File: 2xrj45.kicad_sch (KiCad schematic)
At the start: 20 parts, among them J1 Bus_RJ45_JTH-0024NL, J2 Bus_RJ45_JTH-0024NL

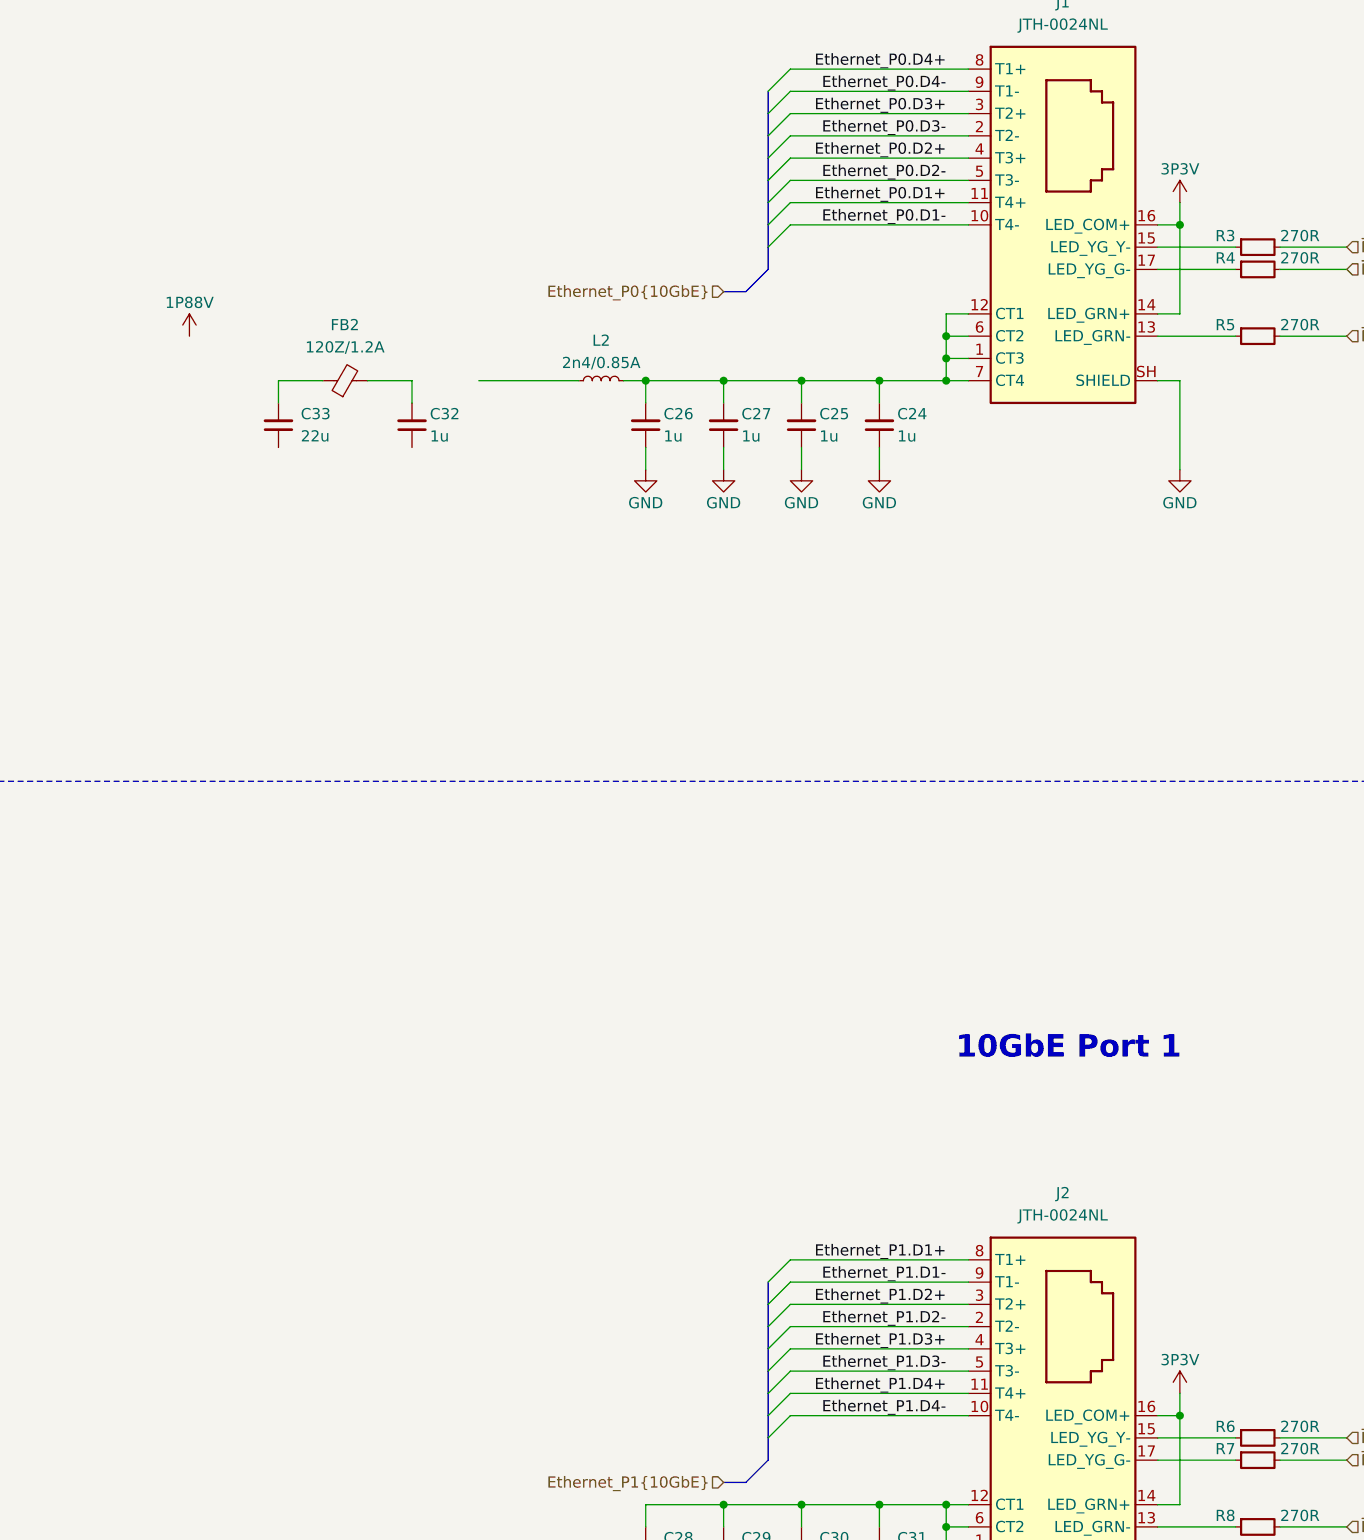
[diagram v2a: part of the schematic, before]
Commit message: [#80813] Change 3V3 and 1V88 power rails names
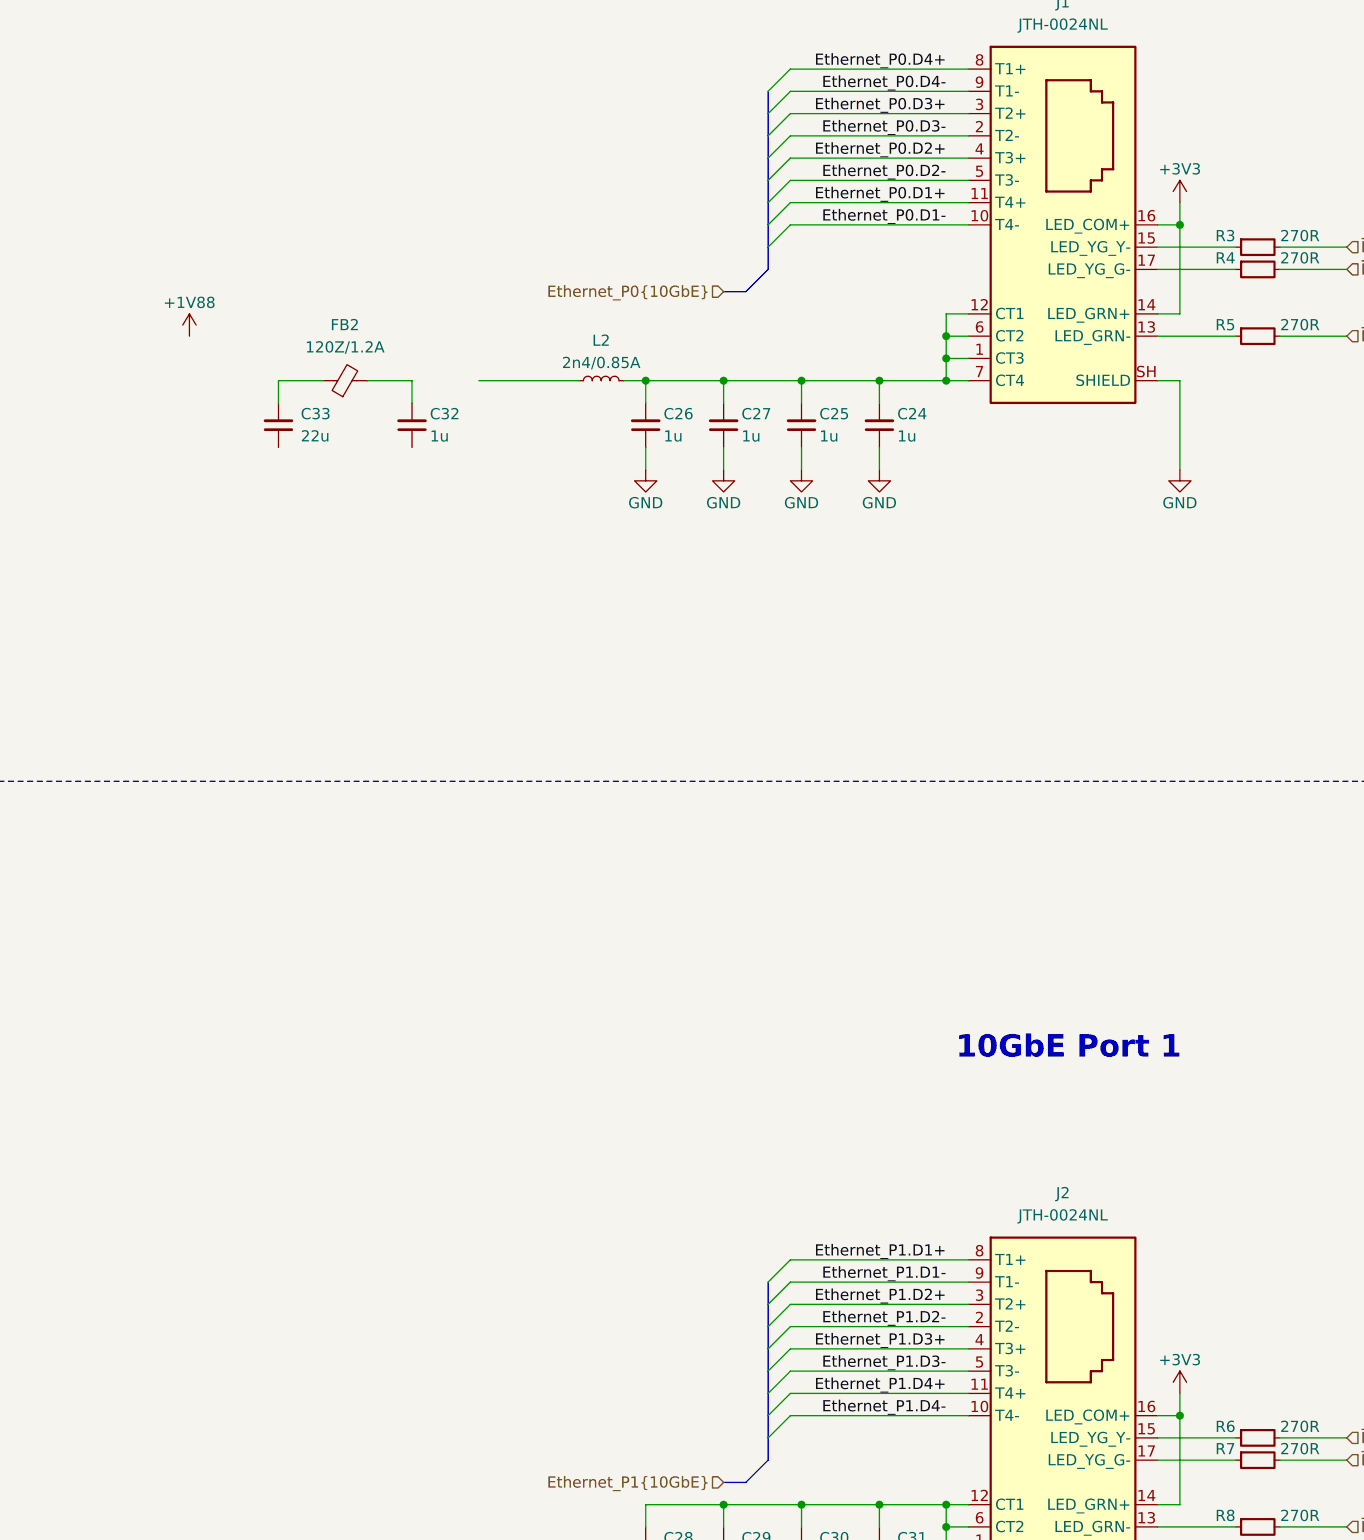
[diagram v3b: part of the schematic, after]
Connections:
- net 3P3V renamed +3V3
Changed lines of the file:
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@@
-	)
-	(symbol
-		(lib_id "antmicropower:VDD")
-		(at 115.57 92.71 0)
-		(unit 1)
-		(exclude_from_sim no)
-		(in_bom yes)
-		(on_board yes)
-		(dnp no)
-		(property "Reference" "#PWR0127"
-			(at 115.57 96.52 0)
-			(effects
-				(font
-					(size 1.27 1.27)
-				)
-				(hide yes)
-			)
-		)
-		(property "Value" "1P88V"
-			(at 115.57 88.9 0)
-			(effects
-				(font
-					(size 1.27 1.27)
-				)
-			)
-		)
-		(property "Footprint" ""
-			(at 115.57 92.71 0)
-			(effects
-				(font
-					(size 1.27 1.27)
-				)
-				(hide yes)
-			)
-		)
-		(property "Datasheet" ""
-			(at 115.57 92.71 0)
-			(effects
-				(font
-					(size 1.27 1.27)
-				)
-				(hide yes)
-			)
-		)
-		(property "Description" ""
-			(at 115.57 92.71 0)
-			(effects
-				(font
-					(size 1.27 1.27)
-				)
-				(hide yes)
-			)
-		)
-		(pin "1"
-		)
-		(instances
-			(project "10-gbe-expansion"
-				(path "/04bda987-e5eb-48b4-9e90-d8211dc11b39/b3dd2e9f-aefc-4b19-a6a4-069fdee319cd"
-					(reference "#PWR0127")
-					(unit 1)
-				)
-			)
-		)
 	)
 	(symbol
@@
 	)
 	(symbol
-		(lib_id "antmicropower:VCC")
-		(at 228.6 77.47 0)
+		(lib_id "antmicropower:+1V8")
+		(at 115.57 92.71 0)
 		(unit 1)
 		(exclude_from_sim no)
@@
 		(on_board yes)
 		(dnp no)
-		(property "Reference" "#PWR04"
-			(at 228.6 81.28 0)
-			(effects
-				(font
-					(size 1.27 1.27)
-				)
-				(hide yes)
-			)
-		)
-		(property "Value" "3P3V"
-			(at 228.6 73.66 0)
-			(effects
-				(font
-					(size 1.27 1.27)
+		(property "Reference" "#PWR014"
+			(at 130.81 95.25 0)
+			(effects
+				(font
+					(size 1.27 1.27)
+					(thickness 0.15)
+				)
+				(justify left bottom)
+				(hide yes)
+			)
+		)
+		(property "Value" "+1V88"
+			(at 115.57 88.9 0)
+			(effects
+				(font
+					(size 1.27 1.27)
+					(thickness 0.15)
 				)
 			)
 		)
 		(property "Footprint" ""
-			(at 228.6 77.47 0)
-			(effects
-				(font
-					(size 1.27 1.27)
-				)
+			(at 130.81 100.33 0)
+			(effects
+				(font
+					(size 1.27 1.27)
+					(thickness 0.15)
+				)
+				(justify left bottom)
 				(hide yes)
 			)
 		)
 		(property "Datasheet" ""
-			(at 228.6 77.47 0)
-			(effects
-				(font
-					(size 1.27 1.27)
-				)
+			(at 130.81 102.87 0)
+			(effects
+				(font
+					(size 1.27 1.27)
+					(thickness 0.15)
+				)
+				(justify left bottom)
 				(hide yes)
 			)
 		)
 		(property "Description" ""
-			(at 228.6 77.47 0)
-			(effects
-				(font
-					(size 1.27 1.27)
-				)
+			(at 115.57 92.71 0)
+			(effects
+				(font
+					(size 1.27 1.27)
+				)
+				(hide yes)
+			)
+		)
+		(property "Author" "Antmicro"
+			(at 130.81 97.79 0)
+			(effects
+				(font
+					(size 1.27 1.27)
+					(thickness 0.15)
+				)
+				(justify left bottom)
+				(hide yes)
+			)
+		)
+		(property "License" "Apache-2.0"
+			(at 130.81 100.33 0)
+			(effects
+				(font
+					(size 1.27 1.27)
+					(thickness 0.15)
+				)
+				(justify left bottom)
 				(hide yes)
 			)
@@
 			(project "10-gbe-expansion"
 				(path "/04bda987-e5eb-48b4-9e90-d8211dc11b39/b3dd2e9f-aefc-4b19-a6a4-069fdee319cd"
-					(reference "#PWR04")
+					(reference "#PWR014")
 					(unit 1)
 				)
@@
 	)
 	(symbol
+		(lib_id "antmicropower:+3V3")
+		(at 228.6 213.36 0)
+		(unit 1)
+		(exclude_from_sim no)
+		(in_bom yes)
+		(on_board yes)
+		(dnp no)
+		(property "Reference" "#PWR04"
+			(at 243.84 213.36 0)
+			(effects
+				(font
+					(size 1.27 1.27)
+					(thickness 0.15)
+				)
+				(justify left bottom)
+				(hide yes)
+			)
+		)
+		(property "Value" "+3V3"
+			(at 228.6 209.55 0)
+			(effects
+				(font
+					(size 1.27 1.27)
+					(thickness 0.15)
+				)
+			)
+		)
+		(property "Footprint" ""
+			(at 243.84 220.98 0)
+			(effects
+				(font
+					(size 1.27 1.27)
+					(thickness 0.15)
+				)
+				(justify left bottom)
+				(hide yes)
+			)
+		)
+		(property "Datasheet" ""
+			(at 243.84 223.52 0)
+			(effects
+				(font
+					(size 1.27 1.27)
+					(thickness 0.15)
+				)
+				(justify left bottom)
+				(hide yes)
+			)
+		)
+		(property "Description" ""
+			(at 228.6 213.36 0)
+			(effects
+				(font
+					(size 1.27 1.27)
+				)
+				(hide yes)
+			)
+		)
+		(property "Author" "Antmicro"
+			(at 243.84 215.9 0)
+			(effects
+				(font
+					(size 1.27 1.27)
+					(thickness 0.15)
+				)
+				(justify left bottom)
+				(hide yes)
+			)
+		)
+		(property "License" "Apache-2.0"
+			(at 243.84 218.44 0)
+			(effects
+				(font
+					(size 1.27 1.27)
+					(thickness 0.15)
+				)
+				(justify left bottom)
+				(hide yes)
+			)
+		)
+		(pin "1"
+		)
+		(instances
+			(project "10-gbe-expansion"
+				(path "/04bda987-e5eb-48b4-9e90-d8211dc11b39/b3dd2e9f-aefc-4b19-a6a4-069fdee319cd"
+					(reference "#PWR04")
+					(unit 1)
+				)
+			)
+		)
+	)
+	(symbol
 		(lib_id "antmicroCapacitors0402:C_1u_25V_0402")
 		(at 140.97 105.41 90)
@@
 				(path "/04bda987-e5eb-48b4-9e90-d8211dc11b39/b3dd2e9f-aefc-4b19-a6a4-069fdee319cd"
 					(reference "C32")
-					(unit 1)
-				)
-			)
-		)
-	)
-	(symbol
-		(lib_id "antmicropower:VCC")
-		(at 228.6 213.36 0)
-		(unit 1)
-		(exclude_from_sim no)
-		(in_bom yes)
-		(on_board yes)
-		(dnp no)
-		(property "Reference" "#PWR06"
-			(at 228.6 217.17 0)
-			(effects
-				(font
-					(size 1.27 1.27)
-				)
-				(hide yes)
-			)
-		)
-		(property "Value" "3P3V"
-			(at 228.6 209.55 0)
-			(effects
-				(font
-					(size 1.27 1.27)
-				)
-			)
-		)
-		(property "Footprint" ""
-			(at 228.6 213.36 0)
-			(effects
-				(font
-					(size 1.27 1.27)
-				)
-				(hide yes)
-			)
-		)
-		(property "Datasheet" ""
-			(at 228.6 213.36 0)
-			(effects
-				(font
-					(size 1.27 1.27)
-				)
-				(hide yes)
-			)
-		)
-		(property "Description" ""
-			(at 228.6 213.36 0)
-			(effects
-				(font
-					(size 1.27 1.27)
-				)
-				(hide yes)
-			)
-		)
-		(pin "1"
-		)
-		(instances
-			(project "10-gbe-expansion"
-				(path "/04bda987-e5eb-48b4-9e90-d8211dc11b39/b3dd2e9f-aefc-4b19-a6a4-069fdee319cd"
-					(reference "#PWR06")
 					(unit 1)
 				)
@@
 					(unit 1)
 				)
+			)
+		)
+	)
+	(symbol
+		(lib_id "antmicropower:+3V3")
+		(at 228.6 77.47 0)
+		(unit 1)
+		(exclude_from_sim no)
+		(in_bom yes)
+		(on_board yes)
+		(dnp no)
+		(property "Reference" "#PWR02"
+			(at 243.84 77.47 0)
+			(effects
+				(font
+					(size 1.27 1.27)
+					(thickness 0.15)
+				)
+				(justify left bottom)
+				(hide yes)
+			)
+		)
+		(property "Value" "+3V3"
+			(at 228.6 73.66 0)
+			(effects
+				(font
+					(size 1.27 1.27)
+					(thickness 0.15)
+				)
+			)
+		)
+		(property "Footprint" ""
+			(at 243.84 85.09 0)
+			(effects
+				(font
+					(size 1.27 1.27)
+					(thickness 0.15)
+				)
+				(justify left bottom)
+				(hide yes)
+			)
+		)
+		(property "Datasheet" ""
+			(at 243.84 87.63 0)
+			(effects
+				(font
+					(size 1.27 1.27)
+					(thickness 0.15)
+				)
+				(justify left bottom)
+				(hide yes)
+			)
+		)
+		(property "Description" ""
+			(at 228.6 77.47 0)
+			(effects
+				(font
+					(size 1.27 1.27)
+				)
+				(hide yes)
+			)
+		)
+		(property "Author" "Antmicro"
+			(at 243.84 80.01 0)
+			(effects
+				(font
+					(size 1.27 1.27)
+					(thickness 0.15)
+				)
+				(justify left bottom)
+				(hide yes)
+			)
+		)
+		(property "License" "Apache-2.0"
+			(at 243.84 82.55 0)
+			(effects
+				(font
+					(size 1.27 1.27)
+					(thickness 0.15)
+				)
+				(justify left bottom)
+				(hide yes)
+			)
+		)
+		(pin "1"
+		)
+		(instances
+			(project "10-gbe-expansion"
+				(path "/04bda987-e5eb-48b4-9e90-d8211dc11b39/b3dd2e9f-aefc-4b19-a6a4-069fdee319cd"
+					(reference "#PWR02")
+					(unit 1)
+				)
